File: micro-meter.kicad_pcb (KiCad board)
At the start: 2 copper layers, 129 parts, among them J1 5V_IN, J2 SPI, J3 I2C / UART, J4 IN1, J5 IN2, J6 IN3, J7 IN4, J8 SWD, J9 USB_B_Micro, U1 XC6206P332MR, U2 STM32F411CEU6, U3 MCP6002-ISN, U4 USBLC6-2SC6, Y1 16MHz

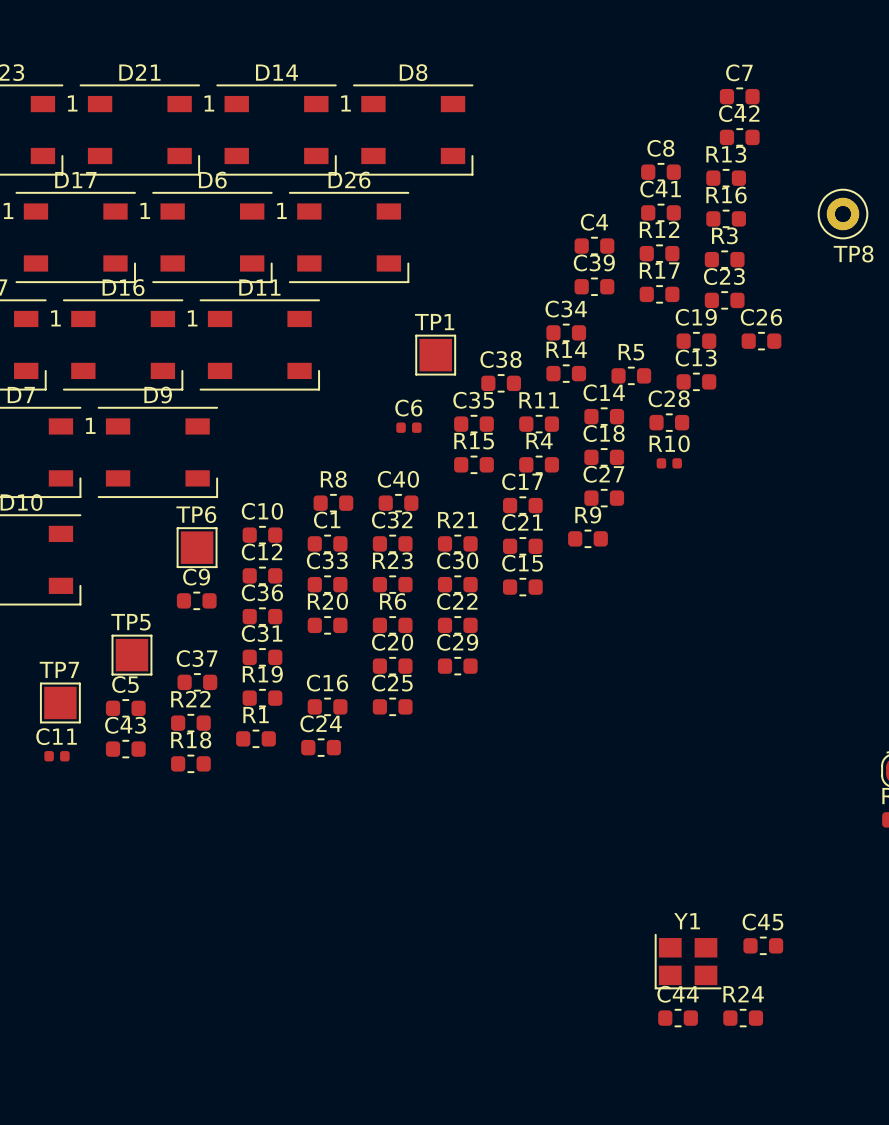
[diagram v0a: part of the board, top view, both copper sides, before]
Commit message: Change to 0402 footprints
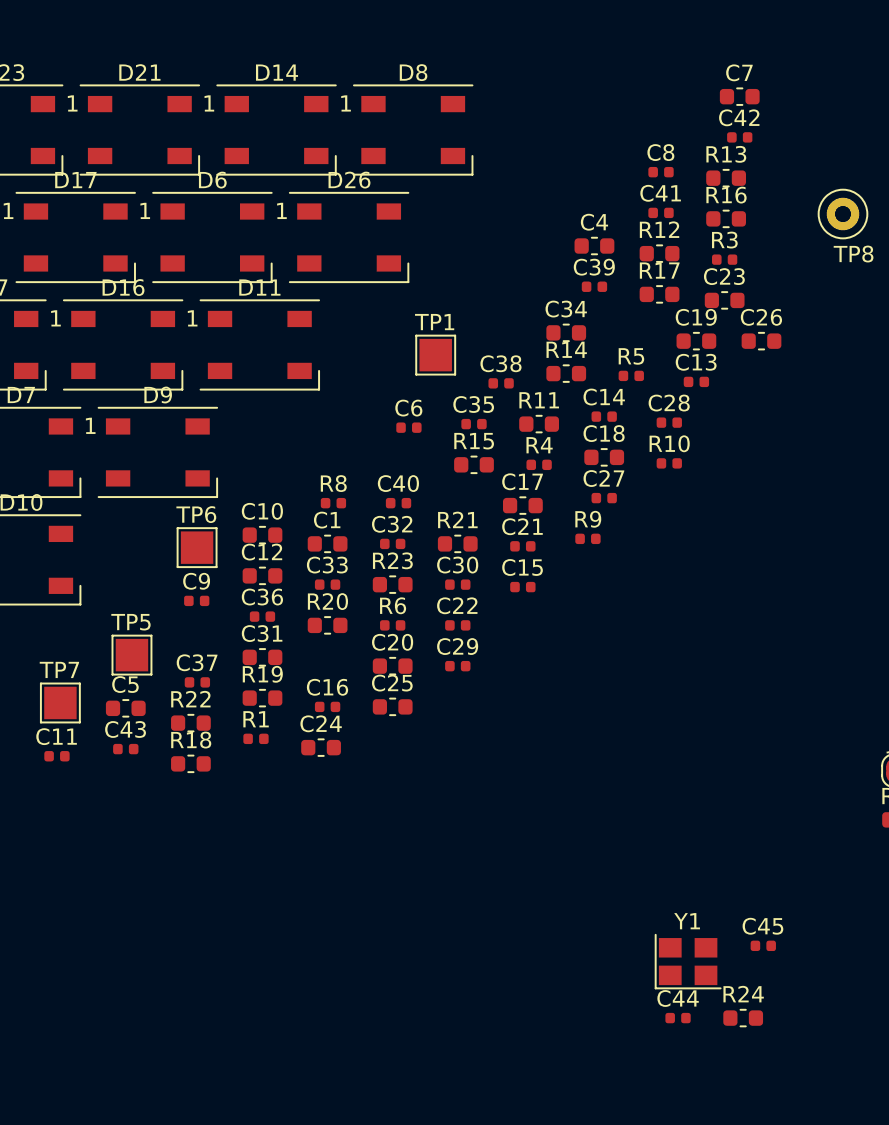
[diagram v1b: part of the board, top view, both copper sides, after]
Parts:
- C13, C14, C15, C16, C21, C22, C27, C28, C29, C30, C32, C33, C35, C36, C37, C38, C39, C40, C41, C42, C43, C44, C45, C8, C9: footprint Capacitor_SMD:C_0603_1608Metric -> Capacitor_SMD:C_0402_1005Metric
- FB1, FB2: footprint Resistor_SMD:R_0805_2012Metric -> Inductor_SMD:L_0805_2012Metric
- R1: value 15k -> 10k; footprint Resistor_SMD:R_0603_1608Metric -> Resistor_SMD:R_0402_1005Metric
- R3, R4, R5, R6, R8, R9: footprint Resistor_SMD:R_0603_1608Metric -> Resistor_SMD:R_0402_1005Metric
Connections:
- net /BOOT0 renamed Net-(R1-Pad1)

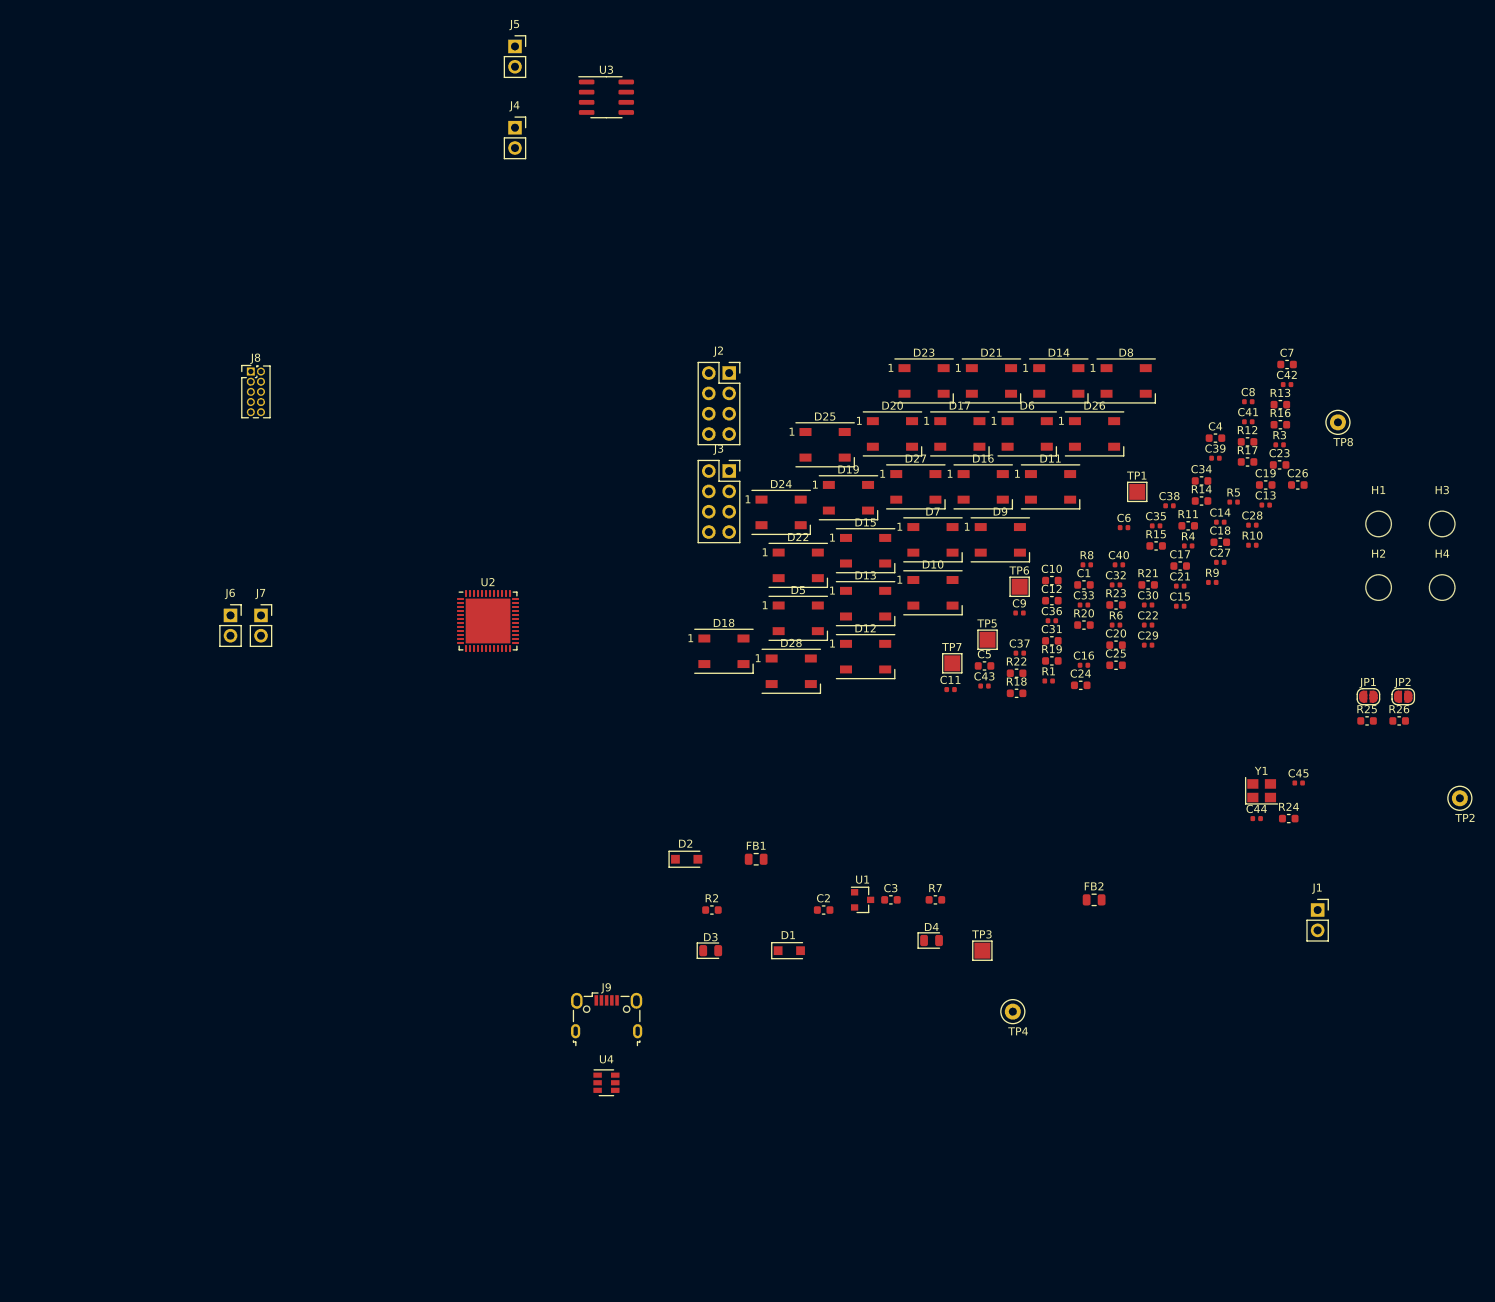
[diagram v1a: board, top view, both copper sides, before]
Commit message: Add buck regulator
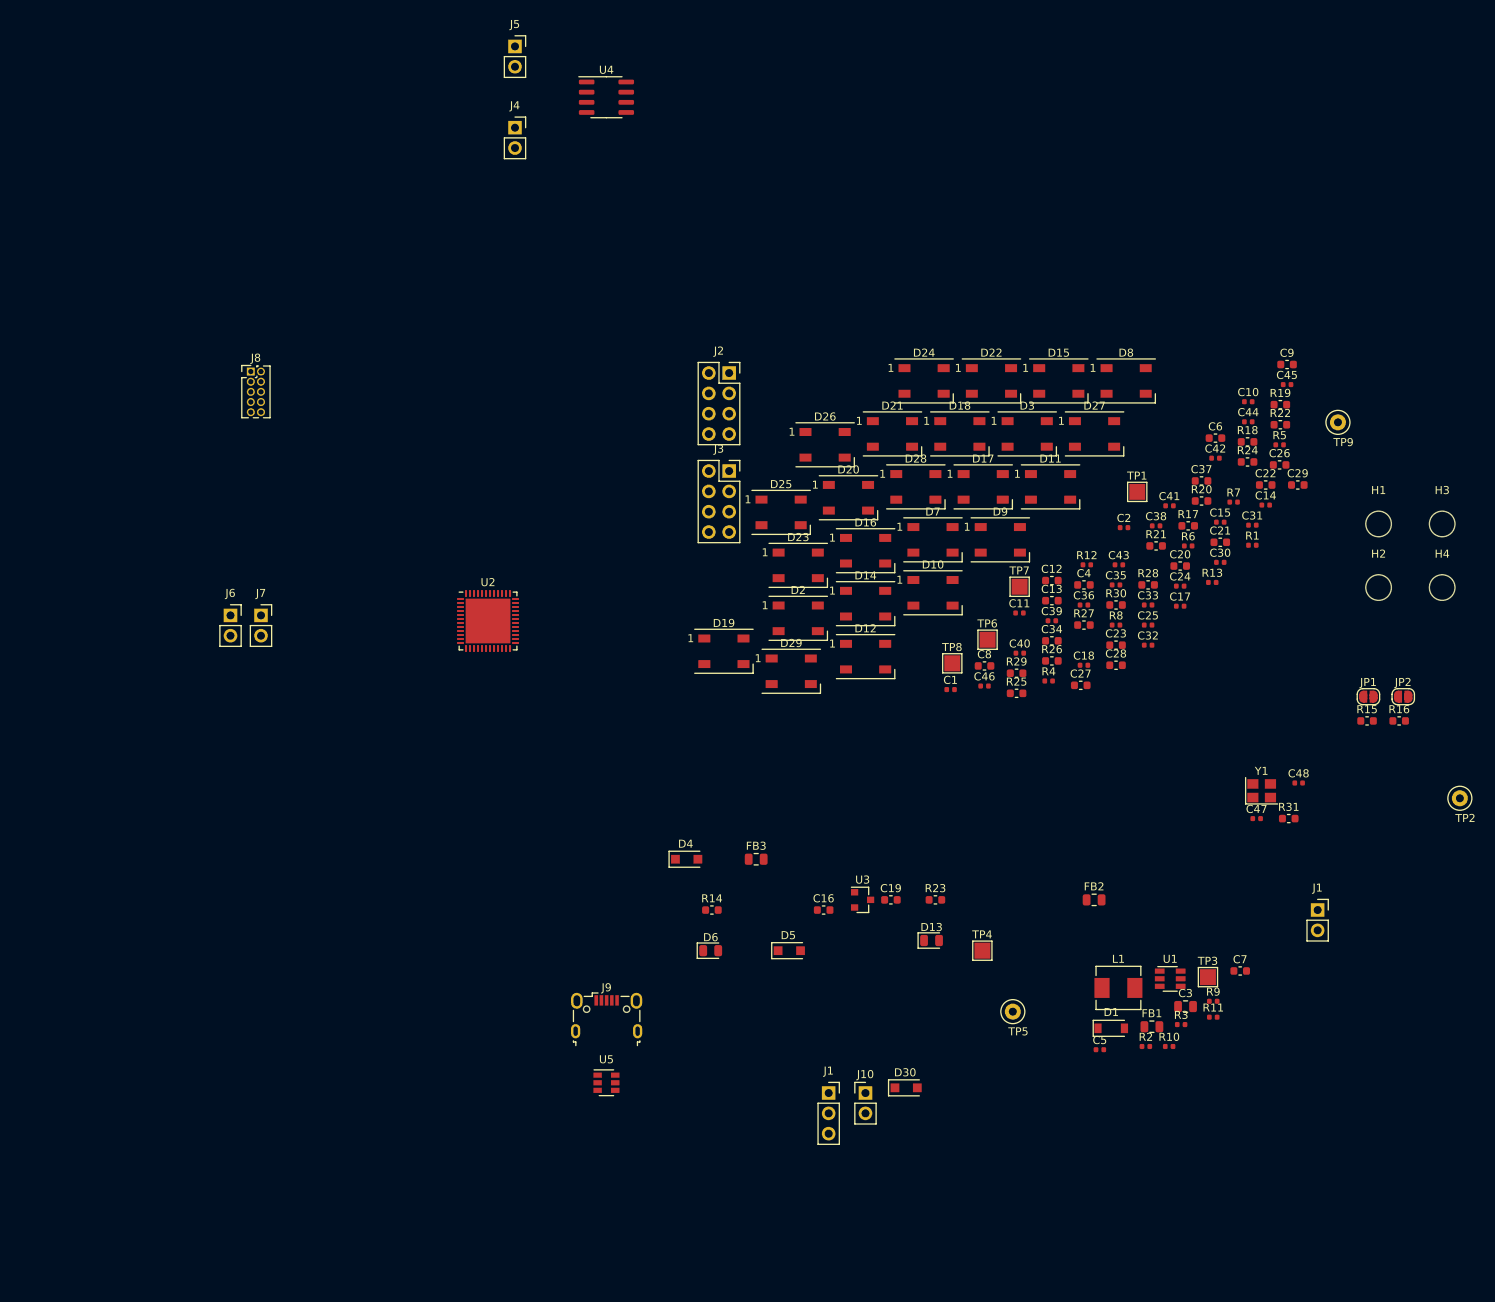
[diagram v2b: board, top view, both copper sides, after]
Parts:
- added C3: 10u, Capacitor_SMD:C_0805_2012Metric, F.Cu at (174.0, 161.9)
- added C5: 10n, Capacitor_SMD:C_0402_1005Metric, F.Cu at (163.3, 167.3)
- added C7: 22u, Capacitor_SMD:C_0603_1608Metric, F.Cu at (180.8, 157.5)
- added D1: B5819W, Diode_SMD:D_SOD-123, F.Cu at (164.7, 164.6)
- added D30: SM4007, Diode_SMD:D_SOD-123F, F.Cu at (139.1, 172.1)
- added FB1: 600@100MHz, Inductor_SMD:L_0805_2012Metric, F.Cu at (169.8, 164.4)
- added J1: DC_IN, Connector_PinSocket_2.54mm:PinSocket_1x03_P2.54mm_Vertical, F.Cu at (129.4, 172.7)
- added J10: 5V_OUT, Connector_PinHeader_2.54mm:PinHeader_1x02_P2.54mm_Vertical, F.Cu at (134.0, 172.7)
- added L1: 10u, Inductor_SMD:L_Sunlord_MWSA0518_5.4x5.2mm, F.Cu at (165.6, 159.6)
- added R10: 15k, Resistor_SMD:R_0402_1005Metric, F.Cu at (171.9, 166.9)
- added R11: 270, Resistor_SMD:R_0402_1005Metric, F.Cu at (177.4, 163.3)
- added R2: 100k, Resistor_SMD:R_0402_1005Metric, F.Cu at (169.0, 166.9)
- added R3: 27k, Resistor_SMD:R_0402_1005Metric, F.Cu at (173.4, 164.2)
- added R9: 47k, Resistor_SMD:R_0402_1005Metric, F.Cu at (177.4, 161.3)
- added TP3: TP_5V, TestPoint:TestPoint_Pad_2.0x2.0mm, F.Cu at (176.8, 158.2)
- added U1: MP2359, Package_TO_SOT_SMD:TSOT-23-6, F.Cu at (172.1, 158.4)
- J1: value 5V_IN -> 12V_IN
- renumbered C11 to C1, C8 to C10, C9 to C11, C10 to C12, C12 to C13, C13 to C14, C14 to C15, C2 to C16, C15 to C17, C16 to C18, C3 to C19, C6 to C2, C17 to C20, C18 to C21, C19 to C22, C20 to C23, C21 to C24, C22 to C25, C23 to C26, C24 to C27, C25 to C28, C26 to C29, C27 to C30, C28 to C31, C29 to C32, C30 to C33, C31 to C34, C32 to C35, C33 to C36, C34 to C37, C35 to C38, C36 to C39, C1 to C4, C37 to C40, C38 to C41, C39 to C42, C40 to C43, C41 to C44, C42 to C45, C43 to C46, C44 to C47, C45 to C48, C4 to C6, C5 to C8, C7 to C9, D4 to D13, D13 to D14, D14 to D15, D15 to D16, D16 to D17, D17 to D18, D18 to D19, D5 to D2, D19 to D20, D20 to D21, D21 to D22, D22 to D23, D23 to D24, D24 to D25, D25 to D26, D26 to D27, D27 to D28, D28 to D29, D6 to D3, D2 to D4, D1 to D5, D3 to D6, FB1 to FB3, R10 to R1, R8 to R12, R9 to R13, R2 to R14, R25 to R15, R26 to R16, R11 to R17, R12 to R18, R13 to R19, R14 to R20, R15 to R21, R16 to R22, R7 to R23, R17 to R24, R18 to R25, R19 to R26, R20 to R27, R21 to R28, R22 to R29, R23 to R30, R24 to R31, R1 to R4, R3 to R5, R4 to R6, R5 to R7, R6 to R8, TP3 to TP4, TP4 to TP5, TP5 to TP6, TP6 to TP7, TP7 to TP8, TP8 to TP9, U1 to U3, U3 to U4, U4 to U5
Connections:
- C1 pad 2: GND -> Net-(C1-Pad2)
- D4 pad 2: Net-(D2-Pad2) (its old number) -> 5V_OUT
- D5 pad 2: VBUS -> 5V_IN
- J1 pad 1: Net-(D2-Pad2) (its old number) -> Net-(FB1-Pad1)
- R1 pad 1: GND -> Net-(C1-Pad2)
- Y1 pad 3: GND -> Net-(C1-Pad2)

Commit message: Cleanup schematic
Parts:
- C3: value 10u -> 10uF/25V

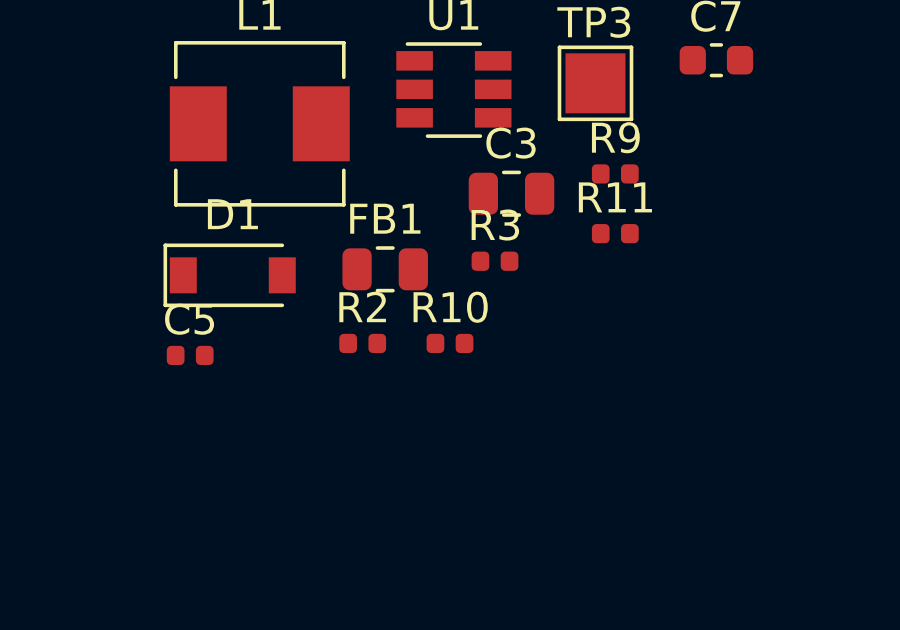
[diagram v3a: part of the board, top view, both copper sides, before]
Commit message: Fix buck reg FB values
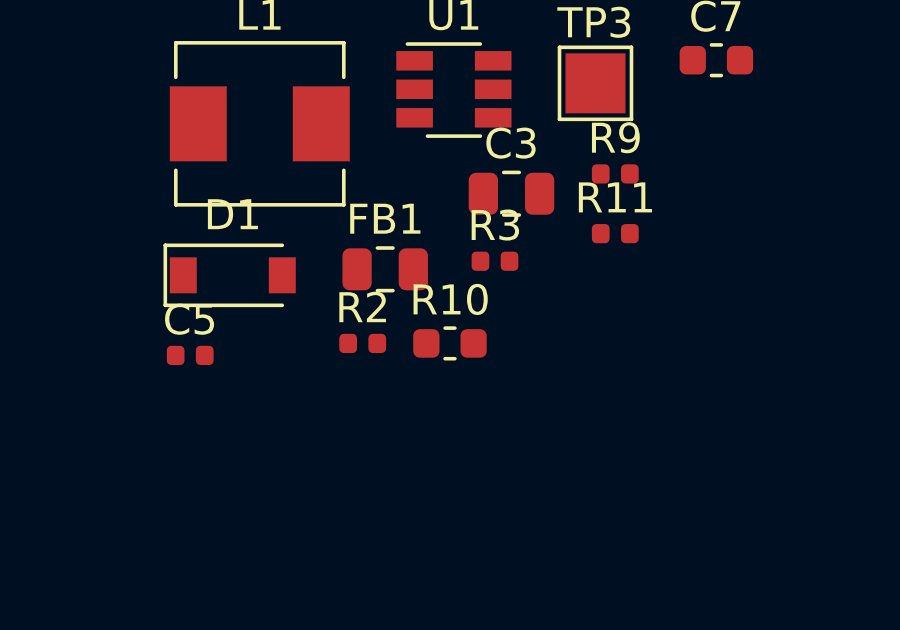
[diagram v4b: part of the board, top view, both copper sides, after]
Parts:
- R10: value 15k -> 9k1; footprint Resistor_SMD:R_0402_1005Metric -> Resistor_SMD:R_0603_1608Metric
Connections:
- R10 pad 1: Net-(R10-Pad1) -> GND
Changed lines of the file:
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@@
     (add_net ~SPI2_CS)
+  )
+  (module Resistor_SMD:R_0603_1608Metric (layer F.Cu)
+    (at 171.94 166.915)
+    (descr "Resistor SMD 0603 (1608 Metric), square (rectangular) end terminal, IPC_7351 nominal, (Body size source: http://www.tortai-tech.com/upload/download/2011102023233369053.pdf), generated with kicad-footprint-generator")
+    (tags resistor)
+    (attr smd)
+    (fp_text reference R10 (at 0 -1.43) (layer F.SilkS)
+      (effects (font (size 1 1) (thickness 0.15)))
+    )
+    (fp_text value 9k1 (at 0 1.43) (layer F.Fab)
+      (effects (font (size 1 1) (thickness 0.15)))
+    )
+    (fp_line (start 1.48 0.73) (end -1.48 0.73) (layer F.CrtYd) (width 0.05))
+    (fp_line (start 1.48 -0.73) (end 1.48 0.73) (layer F.CrtYd) (width 0.05))
+    (fp_line (start -1.48 -0.73) (end 1.48 -0.73) (layer F.CrtYd) (width 0.05))
+    (fp_line (start -1.48 0.73) (end -1.48 -0.73) (layer F.CrtYd) (width 0.05))
+    (fp_line (start -0.162779 0.51) (end 0.162779 0.51) (layer F.SilkS) (width 0.12))
+    (fp_line (start -0.162779 -0.51) (end 0.162779 -0.51) (layer F.SilkS) (width 0.12))
+    (fp_line (start 0.8 0.4) (end -0.8 0.4) (layer F.Fab) (width 0.1))
+    (fp_line (start 0.8 -0.4) (end 0.8 0.4) (layer F.Fab) (width 0.1))
+    (fp_line (start -0.8 -0.4) (end 0.8 -0.4) (layer F.Fab) (width 0.1))
+    (fp_line (start -0.8 0.4) (end -0.8 -0.4) (layer F.Fab) (width 0.1))
+    (fp_text user %R (at 0 0) (layer F.Fab)
+      (effects (font (size 0.4 0.4) (thickness 0.06)))
+    )
+    (pad 2 smd roundrect (at 0.7875 0) (size 0.875 0.95) (layers F.Cu F.Paste F.Mask) (roundrect_rratio 0.25)
+      (net 108 "Net-(R10-Pad2)"))
+    (pad 1 smd roundrect (at -0.7875 0) (size 0.875 0.95) (layers F.Cu F.Paste F.Mask) (roundrect_rratio 0.25)
+      (net 2 GND))
+    (model ${KISYS3DMOD}/Resistor_SMD.3dshapes/R_0603_1608Metric.wrl
+      (at (xyz 0 0 0))
+      (scale (xyz 1 1 1))
+      (rotate (xyz 0 0 0))
+    )
   )
   (module Connector_PinHeader_2.54mm:PinHeader_1x02_P2.54mm_Vertical (layer F.Cu)
@@
     (model ${KISYS3DMOD}/Resistor_SMD.3dshapes/R_0402_1005Metric.wrl
       (at (xyz 0 0 0))
-      (scale (xyz 1 1 1))
-      (rotate (xyz 0 0 0))
-    )
-  )
-  (module Resistor_SMD:R_0402_1005Metric (layer F.Cu)
-    (at 171.94 166.915)
-    (descr "Resistor SMD 0402 (1005 Metric), square (rectangular) end terminal, IPC_7351 nominal, (Body size source: http://www.tortai-tech.com/upload/download/2011102023233369053.pdf), generated with kicad-footprint-generator")
-    (tags resistor)
-    (attr smd)
-    (fp_text reference R10 (at 0 -1.17) (layer F.SilkS)
-      (effects (font (size 1 1) (thickness 0.15)))
-    )
-    (fp_text value 15k (at 0 1.17) (layer F.Fab)
-      (effects (font (size 1 1) (thickness 0.15)))
-    )
-    (fp_line (start -0.5 0.25) (end -0.5 -0.25) (layer F.Fab) (width 0.1))
-    (fp_line (start -0.5 -0.25) (end 0.5 -0.25) (layer F.Fab) (width 0.1))
-    (fp_line (start 0.5 -0.25) (end 0.5 0.25) (layer F.Fab) (width 0.1))
-    (fp_line (start 0.5 0.25) (end -0.5 0.25) (layer F.Fab) (width 0.1))
-    (fp_line (start -0.93 0.47) (end -0.93 -0.47) (layer F.CrtYd) (width 0.05))
-    (fp_line (start -0.93 -0.47) (end 0.93 -0.47) (layer F.CrtYd) (width 0.05))
-    (fp_line (start 0.93 -0.47) (end 0.93 0.47) (layer F.CrtYd) (width 0.05))
-    (fp_line (start 0.93 0.47) (end -0.93 0.47) (layer F.CrtYd) (width 0.05))
-    (fp_text user %R (at 0 0) (layer F.Fab)
-      (effects (font (size 0.25 0.25) (thickness 0.04)))
-    )
-    (pad 2 smd roundrect (at 0.485 0) (size 0.59 0.64) (layers F.Cu F.Paste F.Mask) (roundrect_rratio 0.25)
-      (net 108 "Net-(R10-Pad2)"))
-    (pad 1 smd roundrect (at -0.485 0) (size 0.59 0.64) (layers F.Cu F.Paste F.Mask) (roundrect_rratio 0.25)
-      (net 109 "Net-(R10-Pad1)"))
-    (model ${KISYS3DMOD}/Resistor_SMD.3dshapes/R_0402_1005Metric.wrl
-      (at (xyz 0 0 0))

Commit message: Layout blocks
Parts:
- added J11: LEDS_DATA, Connector_PinHeader_2.54mm:PinHeader_1x03_P2.54mm_Vertical, B.Cu at (66.0, 126.5)
- added J12: LEDS_EXT, Connector_PinHeader_2.54mm:PinHeader_1x03_P2.54mm_Vertical, B.Cu at (137.7, 136.7)
- added TP10: TP_4V3, TestPoint:TestPoint_Pad_2.0x2.0mm, F.Cu at (55.9, 189.5)
- J1 (x2), J10, J2, J3, J4, J5, J6, J7, J8: moved to B.Cu
- moved TP2 148.5 mm to (59.9, 129.5)
- moved R9 144.6 mm to (34.0, 179.7), turned to 90 degrees
- moved C3 143.5 mm to (32.8, 187.3), turned to 270 degrees
- moved R3 143.3 mm to (31.5, 183.9)
- moved C7 143.2 mm to (41.0, 188.6), turned to 180 degrees
- moved FB1 141.4 mm to (30.5, 188.5), turned to 90 degrees
- moved TP9 141.1 mm to (86.9, 181.9)
- moved R10 139.7 mm to (32.8, 179.1), turned to 270 degrees
- moved U1 139.7 mm to (34.5, 182.9), turned to 270 degrees
- moved R2 139.4 mm to (30.9, 185.4), turned to 270 degrees
- moved R5 138.6 mm to (70.1, 168.1)
- moved TP3 134.6 mm to (44.7, 183.9)
- moved J4 134.4 mm to (92.5, 186.4), turned to 270 degrees
- moved C9 132.3 mm to (81.8, 162.3), turned to 270 degrees
- moved D1 131.4 mm to (35.3, 187.7), turned to 270 degrees
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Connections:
- D29 pad 2: Net-(D29-Pad2) -> LEDS_EXT
- J2 pad 3: CE -> CE+I2S2_MCK
